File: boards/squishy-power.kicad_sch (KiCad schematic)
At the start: 92 parts, among them U1 W25N01GVZEIG, U10 FXL4TD245BQX, U11 FXL4TD245BQX, U12 FXL4TD245BQX, U13 FXL4TD245BQX, U14 FXL4TD245BQX, U15 FXL4TD245BQX, U16 FXL4TD245BQX, U17 THVD1452DGSR, U18 THVD1452DGSR, U19 THVD1452DGSR, U20 THVD1452DGSR, U21 THVD1452DGSR, U22 THVD1452DGSR, U23 THVD1452DGSR, U24 THVD1452DGSR, U25 THVD1452DGSR, U26 THVD1452DGSR, U27 THVD1452DGSR, U28 THVD1452DGSR, U29 THVD1452DGSR, U30 THVD1452DGSR, U31 THVD1452DGSR, U32 THVD1452DGSR, U33 THVD1452DGSR, U34 THVD1452DGSR, U4 TLV73312PQDRVRQ1, U5 LP5910-1.8DRVR, U7 TLV755533PDRVR, U8 FXL4TD245BQX, U9 FXL4TD245BQX

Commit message: hardware: a bunch of clean up and the like
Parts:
- renumbered C22 to C10, C51 to C12, C47 to C13, C34 to C14, C29 to C15, C46 to C16, C55 to C17, C25 to C18, C58 to C19, C65 to C2, C63 to C20, C54 to C21, C48 to C22, C59 to C23, C61 to C24, C28 to C25, C57 to C26, C53 to C27, C16 to C28, C23 to C3, C35 to C31, C15 to C33, C17 to C34, C21 to C35, C62 to C36, C12 to C38, C11 to C39, C24 to C4, C20 to C40, C13 to C41, C37 to C42, C50 to C43, C19 to C44, C9 to C46, C52 to C47, C60 to C49, C8 to C5, C39 to C50, C41 to C51, C27 to C53, C26 to C56, C56 to C58, C40 to C59, C14 to C6, C45 to C61, C36 to C62, C38 to C63, C44 to C64, C31 to C65, C32 to C66, C49 to C67, C30 to C68, C33 to C69, C18 to C7, C10 to C8, C64 to C9, TP3 to TP1, TP5 to TP2, TP1 to TP3, TP2 to TP4, TP4 to TP5, U26 to U1, U29 to U10, U10 to U11, U25 to U13, U32 to U15, U11 to U16, U24 to U17, U23 to U18, U8 to U2, U12 to U20, U34 to U21, U13 to U23, U28 to U24, U21 to U25, U1 to U26, U14 to U27, U31 to U28, U20 to U29, U7 to U3, U15 to U30, U19 to U31, U30 to U32, U16 to U33, U18 to U34, U33 to U4, U4 to U5, U27 to U6, U5 to U7, U9 to U8, U17 to U9

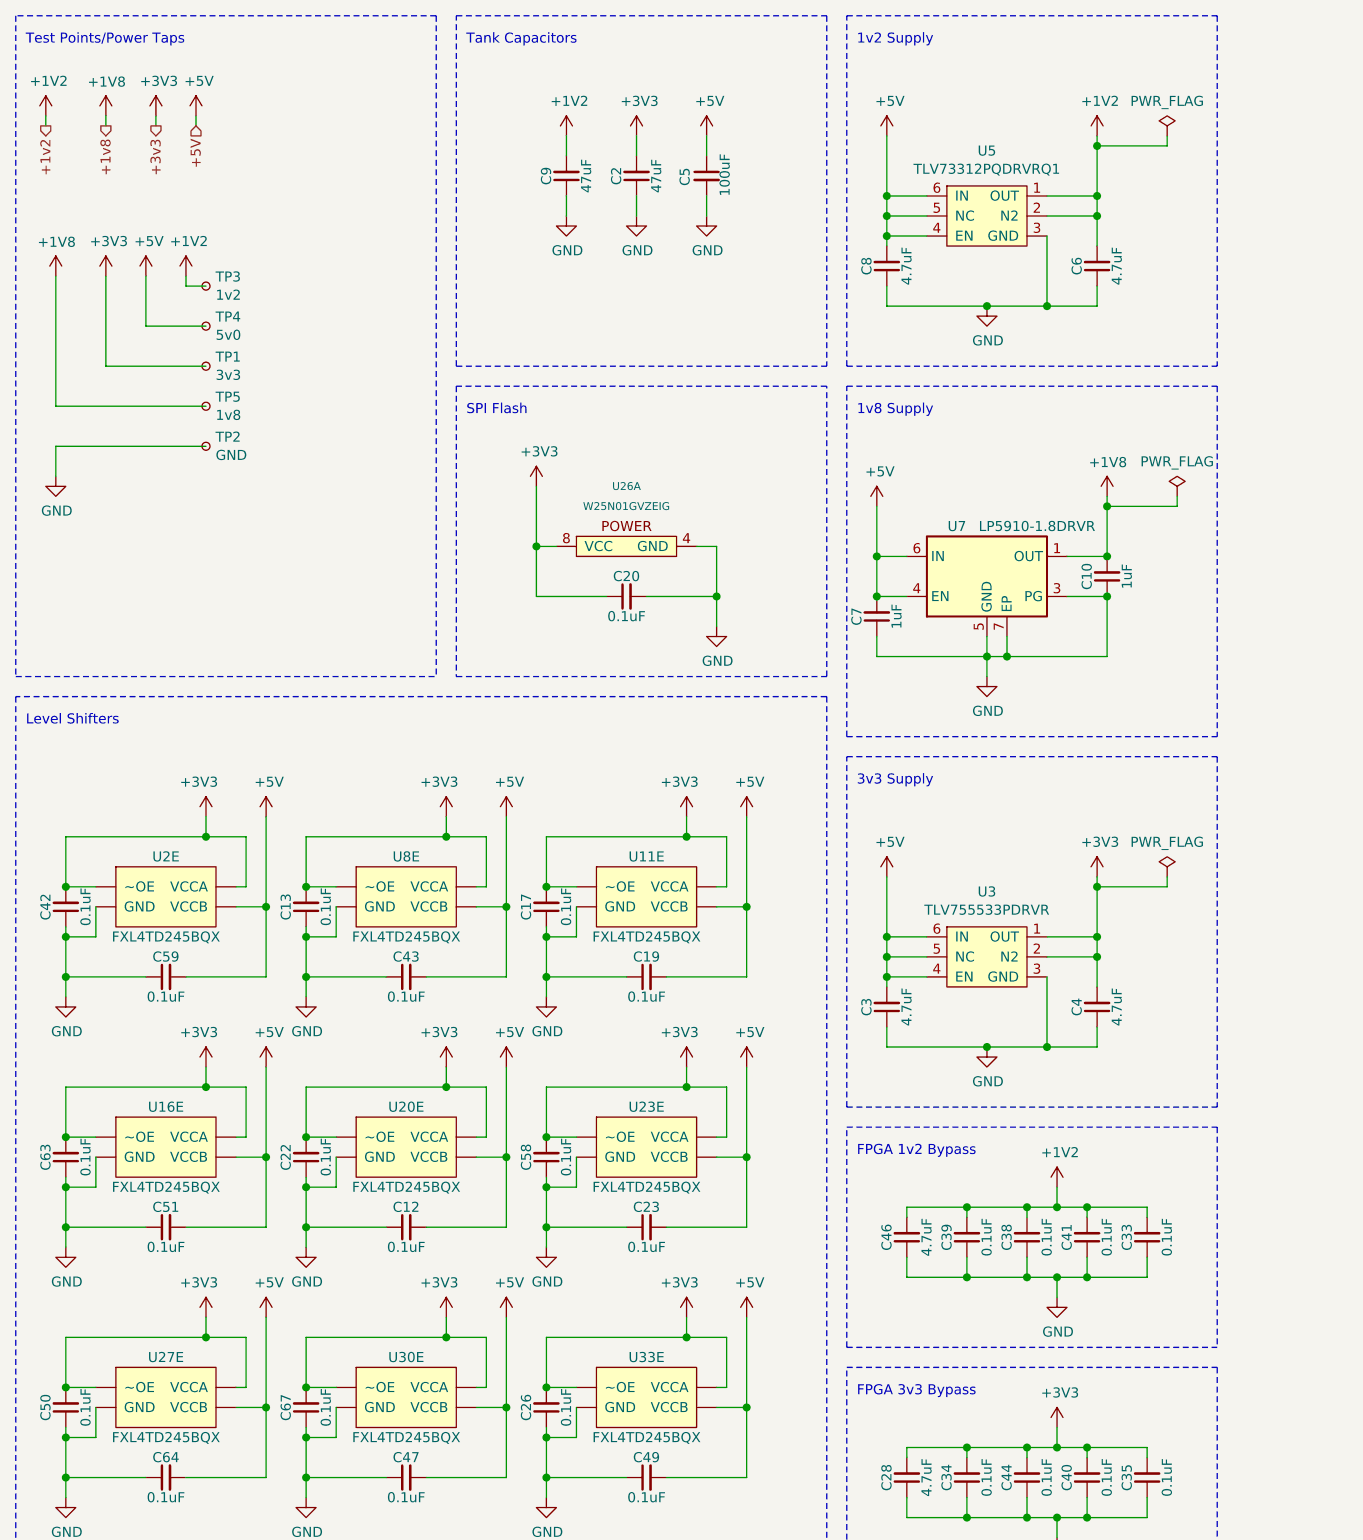
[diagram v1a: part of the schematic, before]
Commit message: hardware: ensured we got a clean bill of health from DRC and ERC
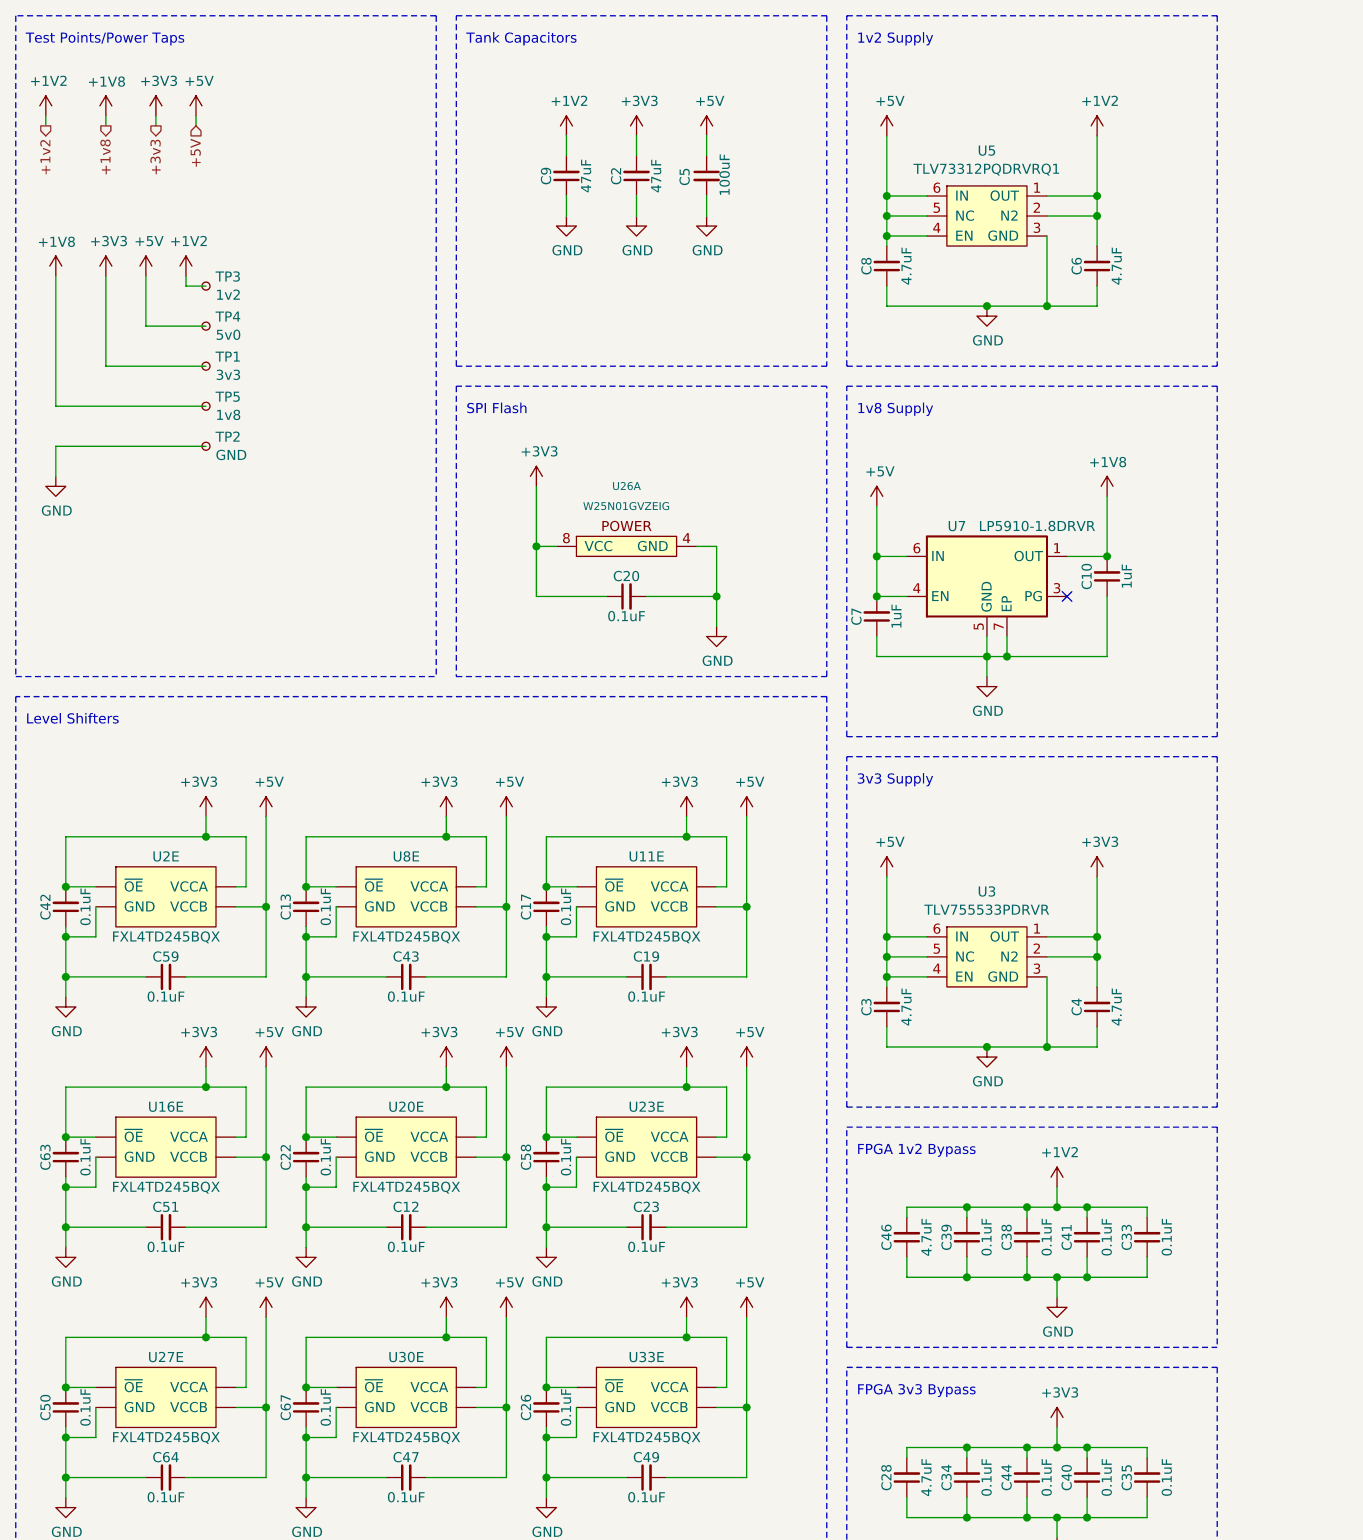
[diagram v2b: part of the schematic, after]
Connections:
- net GND: no longer U7.3 (PG)
- no-connect marks 0 -> 1
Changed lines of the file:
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@@
   (junction (at 149.86 195.58) (diameter 1.016) (color 0 0 0 0))
   (junction (at 149.86 204.47) (diameter 1.016) (color 0 0 0 0))
-  (junction (at 151.13 30.48) (diameter 1.016) (color 0 0 0 0))
   (junction (at 151.13 36.83) (diameter 1.016) (color 0 0 0 0))
   (junction (at 151.13 39.37) (diameter 1.016) (color 0 0 0 0))
-  (junction (at 151.13 124.46) (diameter 1.016) (color 0 0 0 0))
   (junction (at 151.13 130.81) (diameter 1.016) (color 0 0 0 0))
   (junction (at 151.13 133.35) (diameter 1.016) (color 0 0 0 0))
-  (junction (at 152.4 76.2) (diameter 1.016) (color 0 0 0 0))
   (junction (at 152.4 82.55) (diameter 1.016) (color 0 0 0 0))
-  (junction (at 152.4 87.63) (diameter 1.016) (color 0 0 0 0))
   (junction (at 167.64 240.03) (diameter 1.016) (color 0 0 0 0))
   (junction (at 167.64 267.97) (diameter 1.016) (color 0 0 0 0))
@@
   (junction (at 281.94 240.03) (diameter 1.016) (color 0 0 0 0))
   (junction (at 281.94 267.97) (diameter 1.016) (color 0 0 0 0))
+  (no_connect (at 147.32 87.63))
   (wire (pts (xy 17.78 27.94) (xy 17.78 26.67))
     (stroke (width 0) (type solid) (color 0 0 0 0))
@@
     (stroke (width 0) (type solid) (color 0 0 0 0))
   )
-  (wire (pts (xy 147.32 87.63) (xy 152.4 87.63))
-    (stroke (width 0) (type solid) (color 0 0 0 0))
-  )
   (wire (pts (xy 147.32 233.68) (xy 144.78 233.68))
     (stroke (width 0) (type solid) (color 0 0 0 0))
@@
     (stroke (width 0) (type solid) (color 0 0 0 0))
   )
-  (wire (pts (xy 151.13 30.48) (xy 151.13 29.21))
-    (stroke (width 0) (type solid) (color 0 0 0 0))
-  )
-  (wire (pts (xy 151.13 36.83) (xy 151.13 30.48))
+  (wire (pts (xy 151.13 29.21) (xy 151.13 36.83))
     (stroke (width 0) (type solid) (color 0 0 0 0))
   )
@@
     (stroke (width 0) (type solid) (color 0 0 0 0))
   )
-  (wire (pts (xy 151.13 124.46) (xy 151.13 123.19))
-    (stroke (width 0) (type solid) (color 0 0 0 0))
-  )
-  (wire (pts (xy 151.13 130.81) (xy 151.13 124.46))
+  (wire (pts (xy 151.13 123.19) (xy 151.13 130.81))
     (stroke (width 0) (type solid) (color 0 0 0 0))
   )
@@
     (stroke (width 0) (type solid) (color 0 0 0 0))
   )
-  (wire (pts (xy 152.4 76.2) (xy 152.4 74.93))
+  (wire (pts (xy 152.4 74.93) (xy 152.4 82.55))
     (stroke (width 0) (type solid) (color 0 0 0 0))
   )
@@
     (stroke (width 0) (type solid) (color 0 0 0 0))
   )
-  (wire (pts (xy 152.4 82.55) (xy 152.4 76.2))
-    (stroke (width 0) (type solid) (color 0 0 0 0))
-  )
   (wire (pts (xy 152.4 87.63) (xy 152.4 95.25))
     (stroke (width 0) (type solid) (color 0 0 0 0))
@@
   )
   (wire (pts (xy 158.75 267.97) (xy 167.64 267.97))
-    (stroke (width 0) (type solid) (color 0 0 0 0))
-  )
-  (wire (pts (xy 160.02 29.21) (xy 160.02 30.48))
-    (stroke (width 0) (type solid) (color 0 0 0 0))
-  )
-  (wire (pts (xy 160.02 30.48) (xy 151.13 30.48))
-    (stroke (width 0) (type solid) (color 0 0 0 0))
-  )
-  (wire (pts (xy 160.02 123.19) (xy 160.02 124.46))
-    (stroke (width 0) (type solid) (color 0 0 0 0))
-  )
-  (wire (pts (xy 160.02 124.46) (xy 151.13 124.46))
-    (stroke (width 0) (type solid) (color 0 0 0 0))
-  )
-  (wire (pts (xy 161.29 74.93) (xy 161.29 76.2))
-    (stroke (width 0) (type solid) (color 0 0 0 0))
-  )
-  (wire (pts (xy 161.29 76.2) (xy 152.4 76.2))
     (stroke (width 0) (type solid) (color 0 0 0 0))
   )
@@
       (effects (font (size 1.27 1.27)) hide)
     )
-    (pin "1")
-  )
-  (symbol (lib_id "power:PWR_FLAG") (at 160.02 29.21 0) (unit 1)
-    (in_bom yes) (on_board yes)
-    (property "Reference" "#FLG0103" (id 0) (at 160.02 27.305 0)
-      (effects (font (size 1.27 1.27)) hide)
-    )
-    (property "Value" "PWR_FLAG" (id 1) (at 160.02 24.8158 0))
-    (property "Footprint" "" (id 2) (at 160.02 29.21 0)
-      (effects (font (size 1.27 1.27)) hide)
-    )
-    (property "Datasheet" "~" (id 3) (at 160.02 29.21 0)
-      (effects (font (size 1.27 1.27)) hide)
-    )
-    (pin "1")
-  )
-  (symbol (lib_id "power:PWR_FLAG") (at 160.02 123.19 0) (unit 1)
-    (in_bom yes) (on_board yes)
-    (property "Reference" "#FLG0102" (id 0) (at 160.02 121.285 0)
-      (effects (font (size 1.27 1.27)) hide)
-    )
-    (property "Value" "PWR_FLAG" (id 1) (at 160.02 118.7958 0))
-    (property "Footprint" "" (id 2) (at 160.02 123.19 0)
-      (effects (font (size 1.27 1.27)) hide)
-    )
-    (property "Datasheet" "~" (id 3) (at 160.02 123.19 0)
-      (effects (font (size 1.27 1.27)) hide)
-    )
-    (pin "1")
-  )
-  (symbol (lib_id "power:PWR_FLAG") (at 161.29 74.93 0) (unit 1)
-    (in_bom yes) (on_board yes)
-    (property "Reference" "#FLG0104" (id 0) (at 161.29 73.025 0)
-      (effects (font (size 1.27 1.27)) hide)
-    )
-    (property "Value" "PWR_FLAG" (id 1) (at 161.29 70.5358 0))
-    (property "Footprint" "" (id 2) (at 161.29 74.93 0)
-      (effects (font (size 1.27 1.27)) hide)
-    )
-    (property "Datasheet" "~" (id 3) (at 161.29 74.93 0)
-      (effects (font (size 1.27 1.27)) hide)
-    )

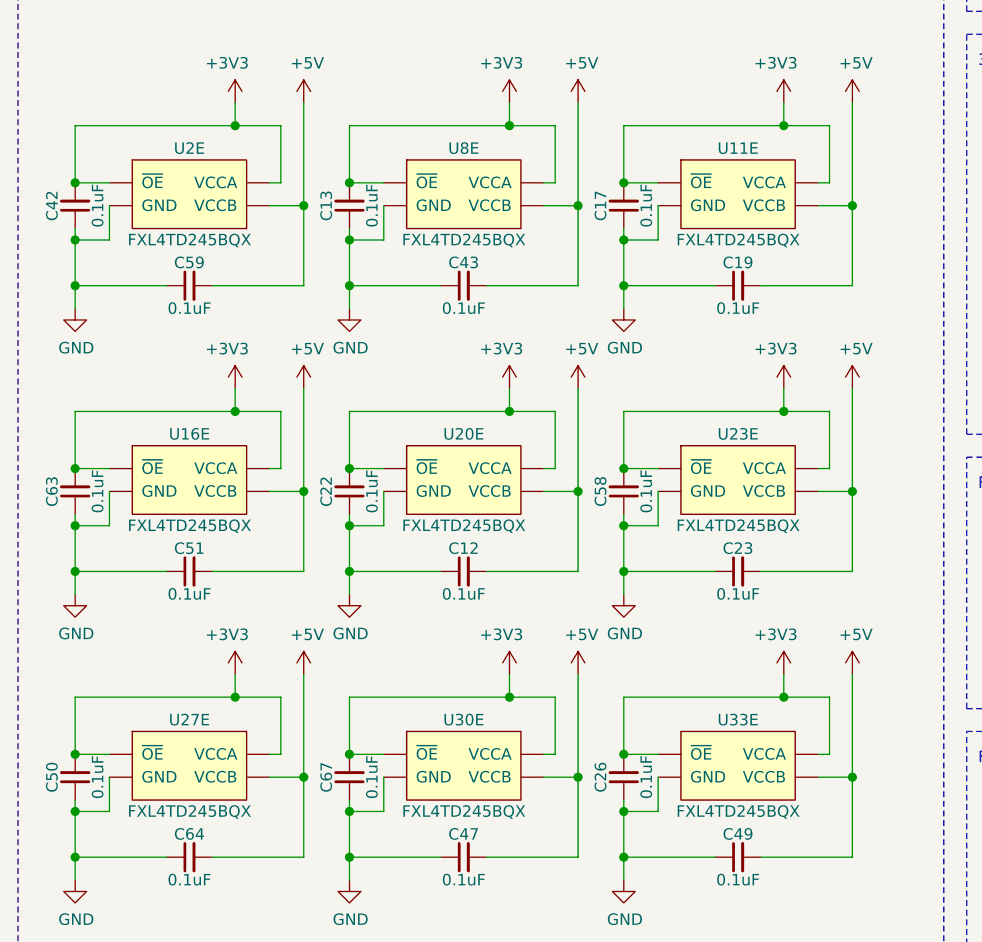
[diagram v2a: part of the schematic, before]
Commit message: hardware: fixed up some datasheets for symbols and added mounting holes
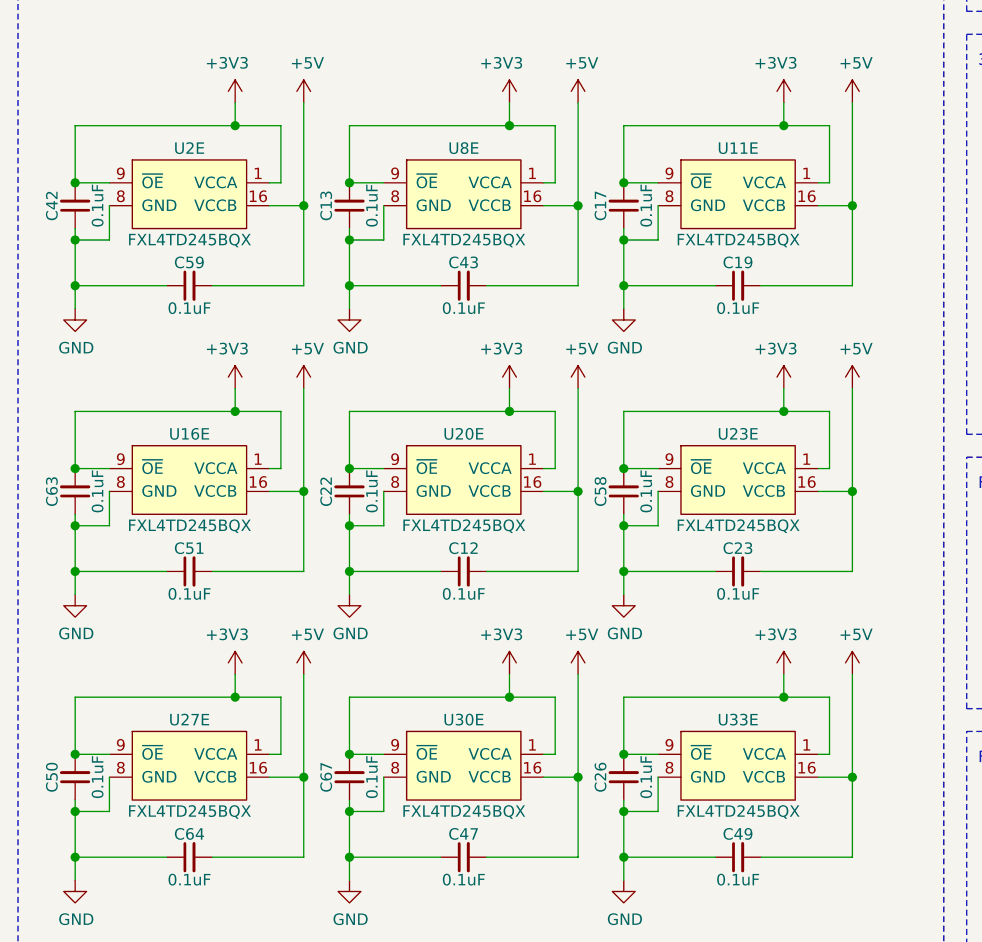
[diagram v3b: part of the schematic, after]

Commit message: hardware: ensured all of the parts had a mpn and mfr
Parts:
- C10, C7: MFR (none) -> Taiyo Yuden; MPN (none) -> UMK107BJ105KA-T
- C2, C9: MFR (none) -> Taiyo Yuden; MPN (none) -> EMK325ABJ476KMHP
- TP1, TP2, TP3, TP4, TP5: MFR (none) -> N/A; MPN (none) -> N/A
- U26: MFR (none) -> Winbond; MPN (none) -> W25N01GVZEIG TR
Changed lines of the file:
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@@
+      (effects (font (size 1.27 1.27)) hide)
+    )
+    (property "MFR" "N/A" (id 4) (at 38.1 48.26 0)
+      (effects (font (size 1.27 1.27)) hide)
+    )
+    (property "MPN" "N/A" (id 5) (at 38.1 48.26 0)
       (effects (font (size 1.27 1.27)) hide)
     )
@@
       (effects (font (size 1.27 1.27)) hide)
     )
+    (property "MFR" "N/A" (id 4) (at 38.1 53.34 0)
+      (effects (font (size 1.27 1.27)) hide)
+    )
+    (property "MPN" "N/A" (id 5) (at 38.1 53.34 0)
+      (effects (font (size 1.27 1.27)) hide)
+    )
     (pin "1")
   )
@@
       (effects (font (size 1.27 1.27)) hide)
     )
+    (property "MFR" "N/A" (id 4) (at 38.1 58.42 0)
+      (effects (font (size 1.27 1.27)) hide)
+    )
+    (property "MPN" "N/A" (id 5) (at 38.1 58.42 0)
+      (effects (font (size 1.27 1.27)) hide)
+    )
     (pin "1")
   )
@@
       (effects (font (size 1.27 1.27)) hide)
     )
+    (property "MFR" "N/A" (id 4) (at 38.1 63.5 0)
+      (effects (font (size 1.27 1.27)) hide)
+    )
+    (property "MPN" "N/A" (id 5) (at 38.1 63.5 0)
+      (effects (font (size 1.27 1.27)) hide)
+    )
     (pin "1")
   )
@@
     )
     (property "Datasheet" "~" (id 3) (at 43.18 68.58 0)
+      (effects (font (size 1.27 1.27)) hide)
+    )
+    (property "MFR" "N/A" (id 4) (at 38.1 68.58 0)
+      (effects (font (size 1.27 1.27)) hide)
+    )
+    (property "MPN" "N/A" (id 5) (at 38.1 68.58 0)
       (effects (font (size 1.27 1.27)) hide)
     )
@@
       (effects (font (size 1.27 1.27)) hide)
     )
-    (property "Datasheet" "~" (id 3) (at 83.82 34.29 0)
-      (effects (font (size 1.27 1.27)) hide)
-    )
-    (property "MFR" "" (id 4) (at 83.82 34.29 90)
-      (effects (font (size 1.27 1.27)) hide)
-    )
-    (property "MPN" "" (id 5) (at 83.82 34.29 90)
+    (property "Datasheet" "https://ds.yuden.co.jp/TYCOMPAS/eu/detail?pn=EMK325ABJ476KMHP&u=M" (id 3) (at 83.82 34.29 0)
+      (effects (font (size 1.27 1.27)) hide)
+    )
+    (property "MFR" "Taiyo Yuden" (id 4) (at 83.82 34.29 90)
+      (effects (font (size 1.27 1.27)) hide)
+    )
+    (property "MPN" "EMK325ABJ476KMHP" (id 5) (at 83.82 34.29 90)
       (effects (font (size 1.27 1.27)) hide)
     )
@@
       (effects (font (size 1.27 1.27)) hide)
     )
-    (property "Datasheet" "~" (id 3) (at 91.44 87.63 0)
+    (property "Datasheet" "https://content.kemet.com/datasheets/KEM_C1006_X5R_SMD.pdf" (id 3) (at 91.44 87.63 0)
       (effects (font (size 1.27 1.27)) hide)
     )
@@
       (effects (font (size 1.27 1.27)) hide)
     )
-    (property "Datasheet" "~" (id 3) (at 92.71 34.29 0)
-      (effects (font (size 1.27 1.27)) hide)
-    )
-    (property "MFR" "" (id 4) (at 92.71 34.29 90)
-      (effects (font (size 1.27 1.27)) hide)
-    )
-    (property "MPN" "" (id 5) (at 92.71 34.29 90)
+    (property "Datasheet" "https://ds.yuden.co.jp/TYCOMPAS/eu/detail?pn=EMK325ABJ476KMHP&u=M" (id 3) (at 92.71 34.29 0)
+      (effects (font (size 1.27 1.27)) hide)
+    )
+    (property "MFR" "Taiyo Yuden" (id 4) (at 92.71 34.29 90)
+      (effects (font (size 1.27 1.27)) hide)
+    )
+    (property "MPN" "EMK325ABJ476KMHP" (id 5) (at 92.71 34.29 90)
       (effects (font (size 1.27 1.27)) hide)
     )
@@
       (effects (font (size 1.27 1.27)) hide)
     )
-    (property "Datasheet" "~" (id 3) (at 101.6 34.29 0)
+    (property "Datasheet" "https://content.kemet.com/datasheets/KEM_C1006_X5R_SMD.pdf" (id 3) (at 101.6 34.29 0)
       (effects (font (size 1.27 1.27)) hide)
     )
@@
       (effects (font (size 1.27 1.27)) hide)
     )
-    (property "MFR" "" (id 4) (at 123.19 90.17 90)
-      (effects (font (size 1.27 1.27)) hide)
-    )
-    (property "MPN" "" (id 5) (at 123.19 90.17 90)
+    (property "MFR" "Taiyo Yuden" (id 4) (at 123.19 90.17 90)
+      (effects (font (size 1.27 1.27)) hide)
+    )
+    (property "MPN" "UMK107BJ105KA-T" (id 5) (at 123.19 90.17 90)
       (effects (font (size 1.27 1.27)) hide)
     )
@@
       (effects (font (size 1.27 1.27)) hide)
     )
-    (property "MFR" "" (id 4) (at 152.4 85.09 90)
-      (effects (font (size 1.27 1.27)) hide)
-    )
-    (property "MPN" "" (id 5) (at 152.4 85.09 90)
+    (property "MFR" "Taiyo Yuden" (id 4) (at 152.4 85.09 90)
+      (effects (font (size 1.27 1.27)) hide)
+    )
+    (property "MPN" "UMK107BJ105KA-T" (id 5) (at 152.4 85.09 90)
       (effects (font (size 1.27 1.27)) hide)
     )
@@
       (effects (font (size 0.9906 0.9906)) hide)
     )
+    (property "MFR" "Winbond" (id 4) (at 91.44 80.01 0)
+      (effects (font (size 1.27 1.27)) hide)
+    )
+    (property "MPN" "W25N01GVZEIG TR" (id 5) (at 91.44 80.01 0)
+      (effects (font (size 1.27 1.27)) hide)
+    )
     (pin "4")
